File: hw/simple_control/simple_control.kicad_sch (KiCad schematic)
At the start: 8 parts, among them J101 Screw_Terminal_01x02, J102 Jack-DC, J103 Screw_Terminal_01x03, J104 Screw_Terminal_01x03

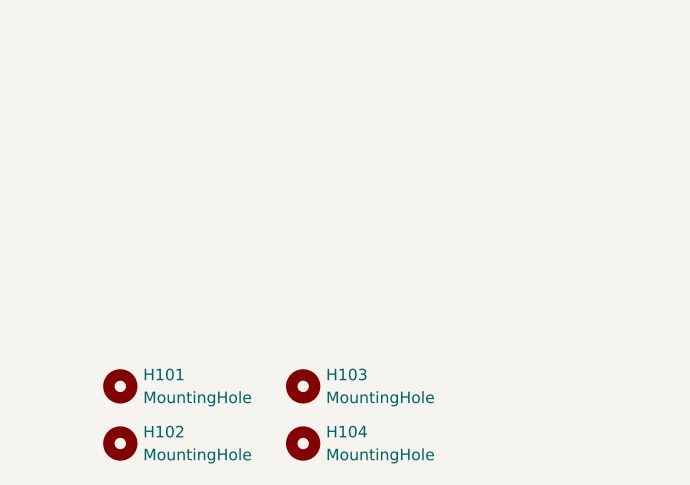
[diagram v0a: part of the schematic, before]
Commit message: chore(hw): add logo and more layout
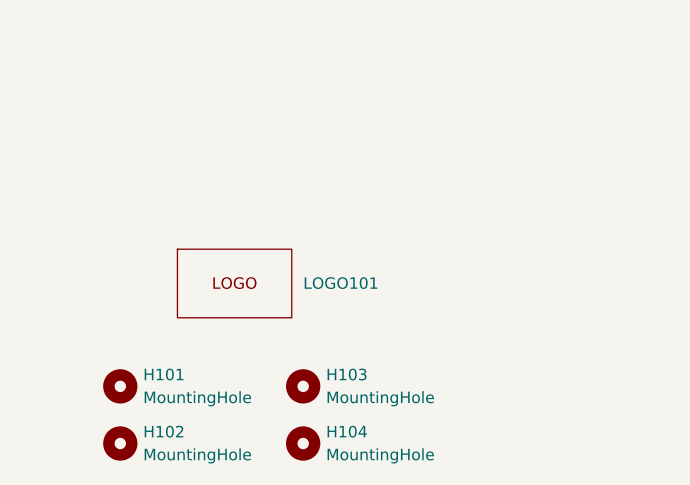
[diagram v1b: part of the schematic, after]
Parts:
- added LOGO101: ~, my:logo, symbol my:Logo
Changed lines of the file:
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@@
+    )
+  )
+  (symbol (lib_id "my:Logo") (at 43.18 151.13 0) (unit 1)
+    (in_bom no) (on_board yes) (dnp no) (fields_autoplaced)
+    (property "Reference" "LOGO101" (at 50.8 151.13 0)
+      (effects (font (size 1.27 1.27)) (justify left))
+    )
+    (property "Value" "~" (at 43.18 151.13 0)
+      (effects (font (size 1.27 1.27)))
+    )
+    (property "Footprint" "my:logo" (at 43.18 156.21 0)
+      (effects (font (size 1.27 1.27)) hide)
+    )
+    (property "Datasheet" "" (at 43.18 151.13 0)
+      (effects (font (size 1.27 1.27)) hide)
+    )
+    (instances
+      (project "simple_control"
+        (path "/063164e8-0d2a-492b-8a61-e4fa4fbf06a6"
+          (reference "LOGO101") (unit 1)
+        )
+      )
     )
   )
